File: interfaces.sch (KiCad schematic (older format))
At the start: 32 parts, among them J17 SM06B-GHS-TB, J20 XBEE, Q11 BSS138DW, Q6 BSS138DW, U13 SN74LV4T125, U19 NC7SZ157, U20 NC7SZ157

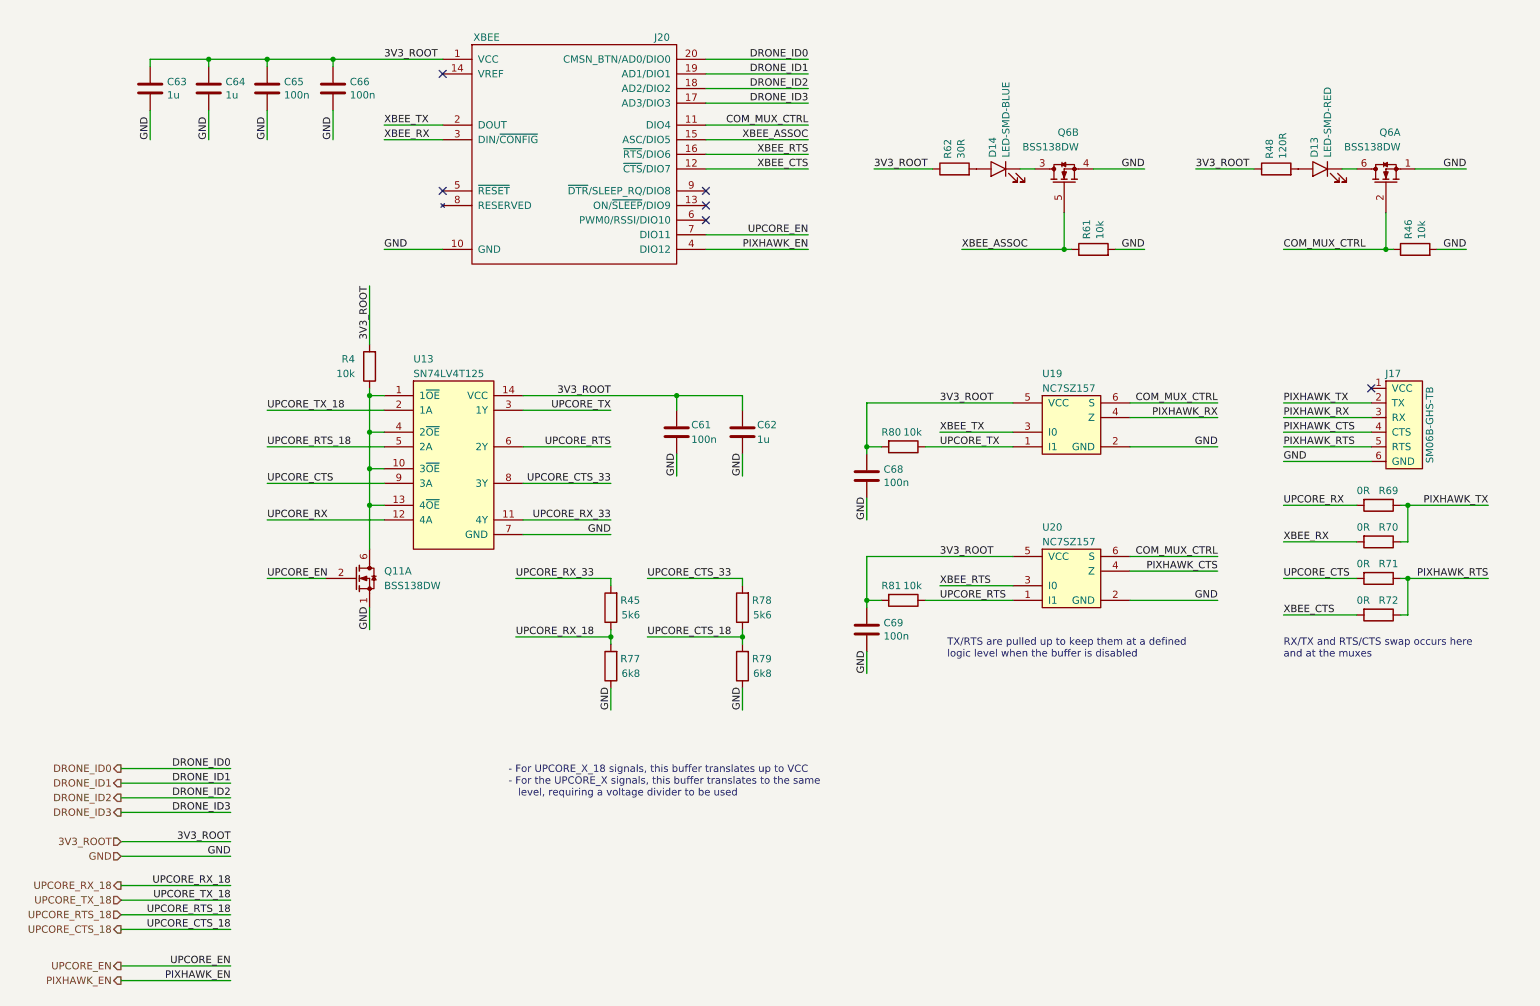
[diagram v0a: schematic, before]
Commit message: Start integrating the new USB hub
1. Remove the two HSIC hubs
2. Create a new schematic (usb.sch) that conserves the PMIC and connectors from the previous design
3. Remove unused GPIO expander and replace with a GPIO-based reset line
4. Add a 25 MHz oscillator for the new hub
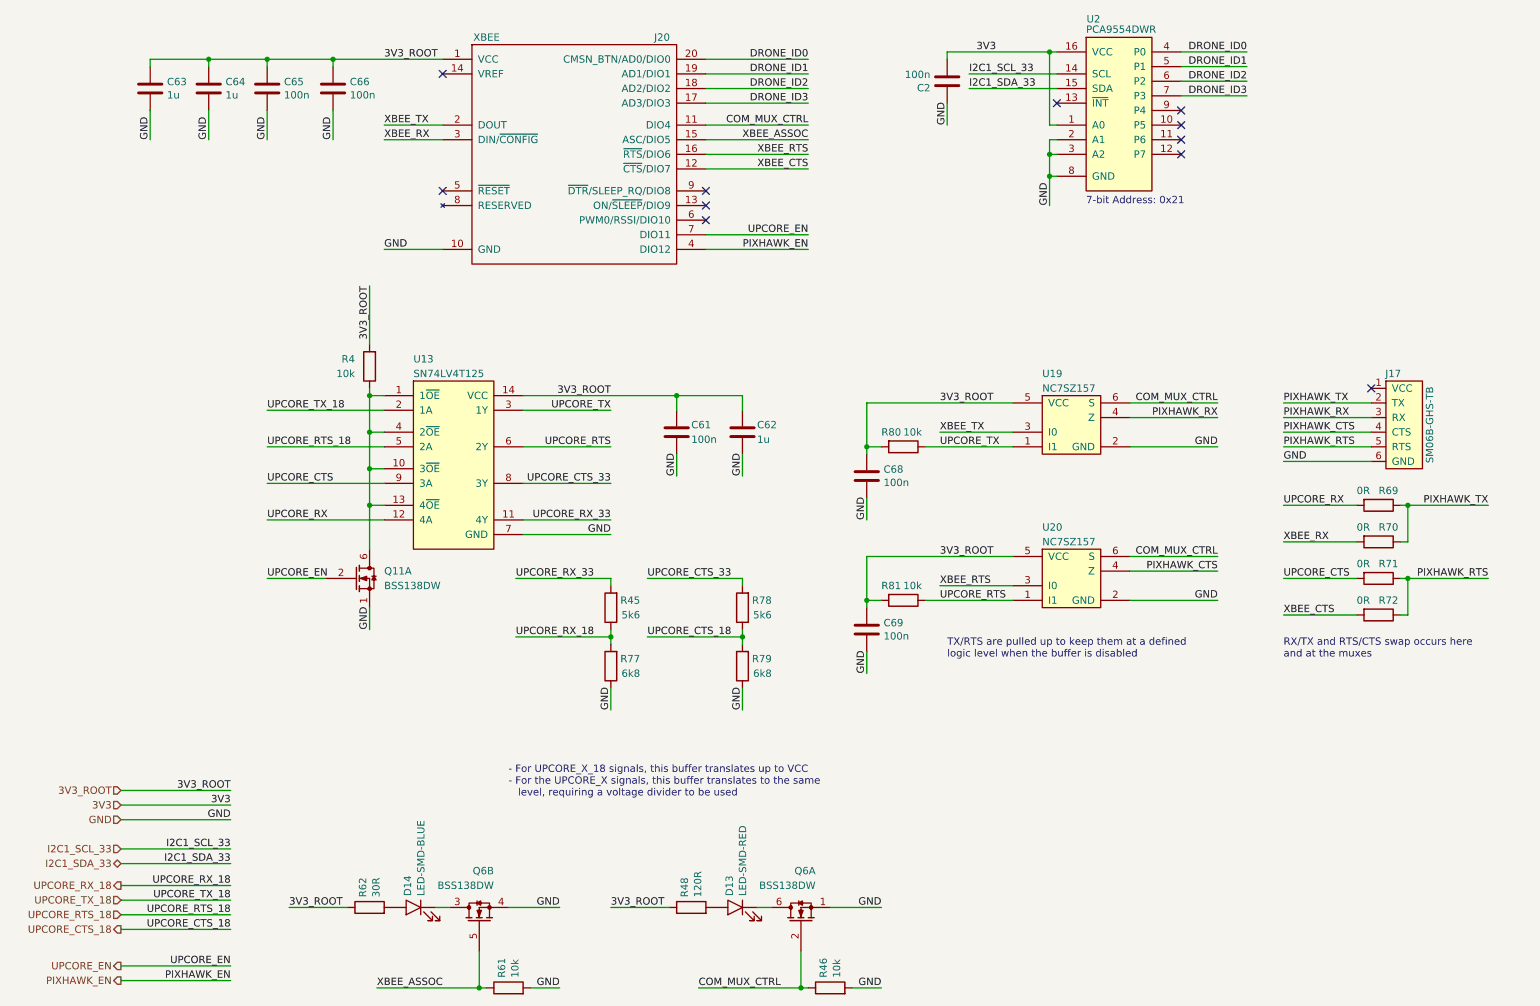
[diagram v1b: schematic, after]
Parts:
- added C2: 100n, Drone:C0805, symbol Drone:CAP
- added U2: PCA9554DWR, Drone:PCA9554DWR, symbol Drone:PCA9554DWR
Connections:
- net DRONE_ID0: now also U2.4 (P0)
- net DRONE_ID1: now also U2.5 (P1)
- net DRONE_ID2: now also U2.6 (P2)
- net DRONE_ID3: now also U2.7 (P3)
- net GND: now also C2.1, U2.2 (A1), U2.3 (A2), U2.8 (GND)
- new net 3V3: C2.2, U2.1 (A0), U2.16 (VCC)
- new net I2C1_SCL_33: U2.14 (SCL)
- new net I2C1_SDA_33: U2.15 (SDA)
- no-connect marks 6 -> 11
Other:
- note added: "7-bit Address: 0x21"
- moved on the sheet: D13, D14, Q6A, Q6B, R46, R48, R61, R62
